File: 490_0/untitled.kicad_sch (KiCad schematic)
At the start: 30 parts, among them J2 BM04B-PASS-1-TFT, J3 BM04B-PASS-1-TFT, U4 USB2512B-I/M2, Y1 24 MHz

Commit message: Changed 8conn and BOM update
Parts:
- C17, C18: footprint (none) -> Capacitor_SMD:C_0603_1608Metric
- C53, C54, C56, C57, C58, C59, C60, C61, C62: footprint (none) -> Capacitor_SMD:C_0805_2012Metric
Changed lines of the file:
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@@
 			)
 		)
-		(property "Footprint" ""
+		(property "Footprint" "Capacitor_SMD:C_0805_2012Metric"
 			(at 177.8 88.9 0)
 			(effects
@@
 			)
 		)
-		(property "Footprint" ""
+		(property "Footprint" "Capacitor_SMD:C_0805_2012Metric"
 			(at 88.9 88.9 0)
 			(effects
@@
 			)
 		)
-		(property "Footprint" ""
+		(property "Footprint" "Capacitor_SMD:C_0805_2012Metric"
 			(at 53.34 88.9 0)
 			(effects
@@
 			)
 		)
-		(property "Footprint" ""
+		(property "Footprint" "Capacitor_SMD:C_0805_2012Metric"
 			(at 81.28 142.24 0)
 			(effects
@@
 			)
 		)
-		(property "Footprint" ""
+		(property "Footprint" "Capacitor_SMD:C_0805_2012Metric"
 			(at 66.04 78.74 0)
 			(effects
@@
 			)
 		)
-		(property "Footprint" ""
+		(property "Footprint" "Capacitor_SMD:C_0805_2012Metric"
 			(at 81.28 137.16 0)
 			(effects
@@
 			)
 		)
-		(property "Footprint" ""
+		(property "Footprint" "Capacitor_SMD:C_0805_2012Metric"
 			(at 73.66 88.9 0)
 			(effects
@@
 			)
 		)
-		(property "Footprint" ""
+		(property "Footprint" "Capacitor_SMD:C_0805_2012Metric"
 			(at 185.42 78.74 0)
 			(effects
@@
 			)
 		)
-		(property "Footprint" ""
+		(property "Footprint" "Capacitor_SMD:C_0603_1608Metric"
 			(at 33.02 152.4 0)
 			(effects
@@
 			)
 		)
-		(property "Footprint" ""
+		(property "Footprint" "Capacitor_SMD:C_0805_2012Metric"
 			(at 81.28 78.74 0)
 			(effects
@@
 			)
 		)
-		(property "Footprint" ""
+		(property "Footprint" "Capacitor_SMD:C_0603_1608Metric"
 			(at 17.78 152.4 0)
 			(effects

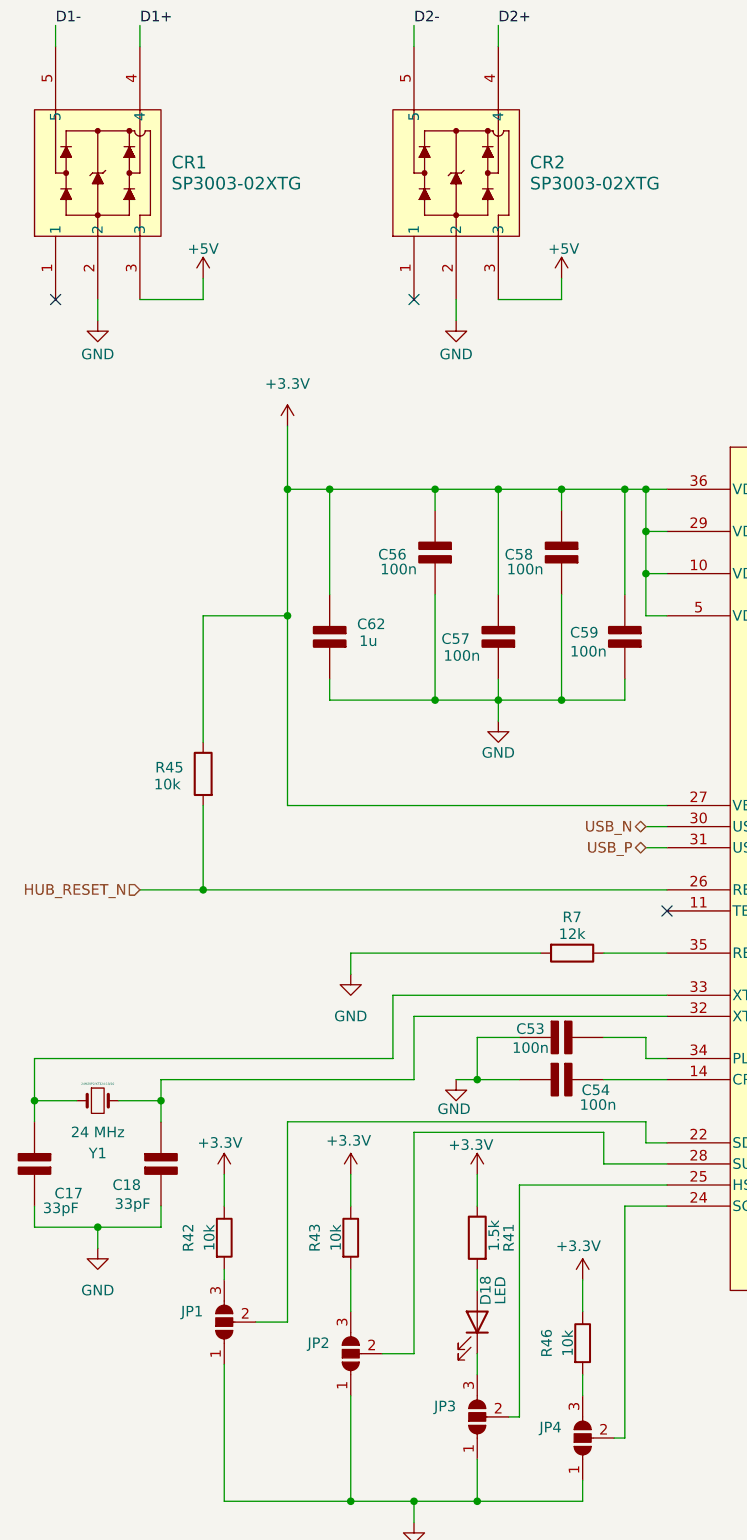
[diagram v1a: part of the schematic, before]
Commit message: LED names + 5V routing through ESD + renamed ESD chips to "U"
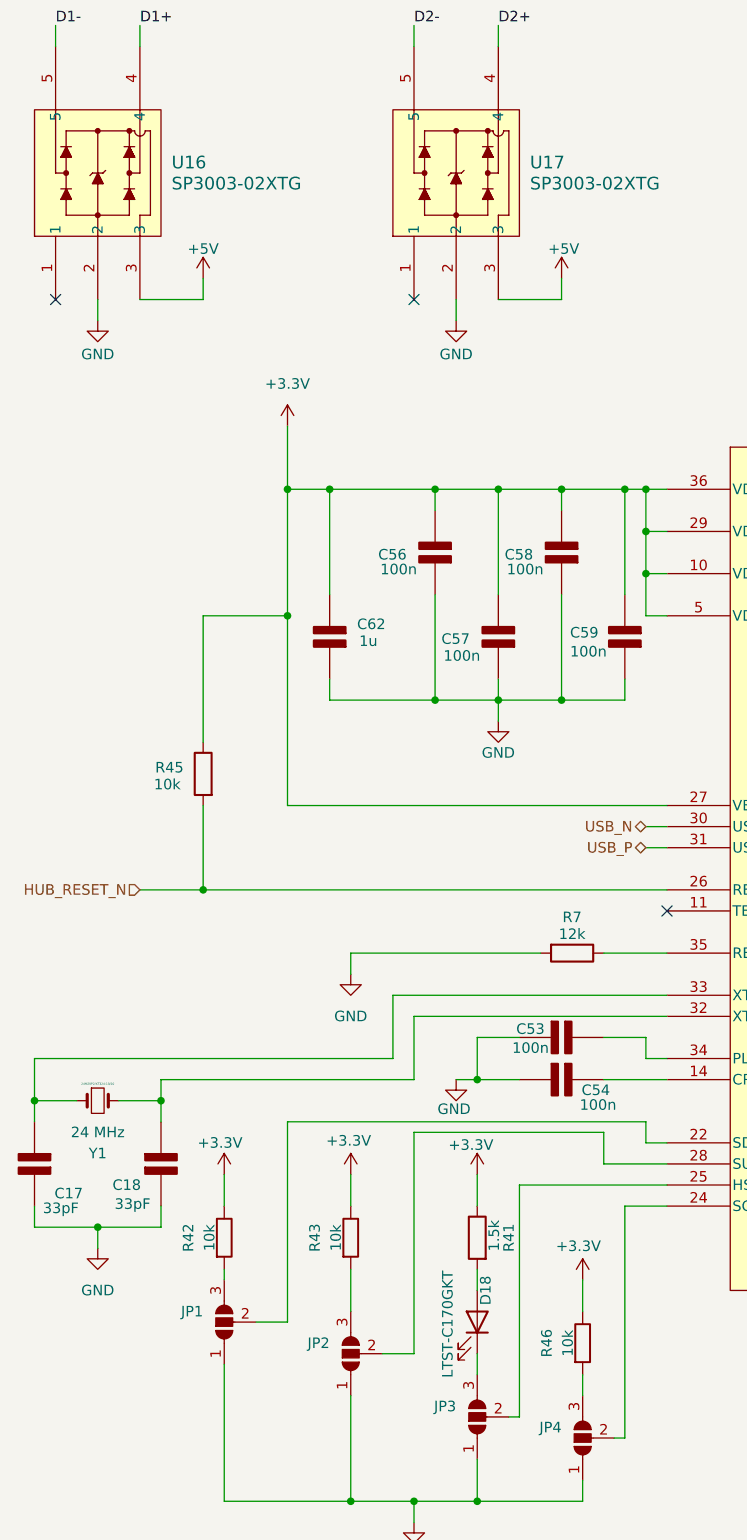
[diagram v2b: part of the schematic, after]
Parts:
- D18: value LED -> LTST-C170GKT
- renumbered CR1 to U16, CR2 to U17
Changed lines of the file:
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@@
 		(dnp no)
 		(fields_autoplaced yes)
-		(property "Reference" "CR1"
+		(property "Reference" "U16"
 			(at 34.29 31.7499 90)
 			(effects
@@
 			(project "490_0"
 				(path "/365a82ed-827d-43e1-aa2f-b98221c4179c/a8971e06-9d2b-4df6-83ab-783791bb1c3f/068f11fb-720d-48b0-8797-6d8a5a01cc51"
-					(reference "CR1")
+					(reference "U16")
 					(unit 1)
 				)
@@
 		(dnp no)
 		(fields_autoplaced yes)
-		(property "Reference" "CR2"
+		(property "Reference" "U17"
 			(at 77.47 31.7499 90)
 			(effects
@@
 			(project "490_0"
 				(path "/365a82ed-827d-43e1-aa2f-b98221c4179c/a8971e06-9d2b-4df6-83ab-783791bb1c3f/068f11fb-720d-48b0-8797-6d8a5a01cc51"
-					(reference "CR2")
+					(reference "U17")
 					(unit 1)
 				)
@@
 			)
 		)
-		(property "Value" "LED"
-			(at 73.914 167.64 0)
+		(property "Value" "LTST-C170GKT"
+			(at 67.564 171.704 0)
 			(effects
 				(font

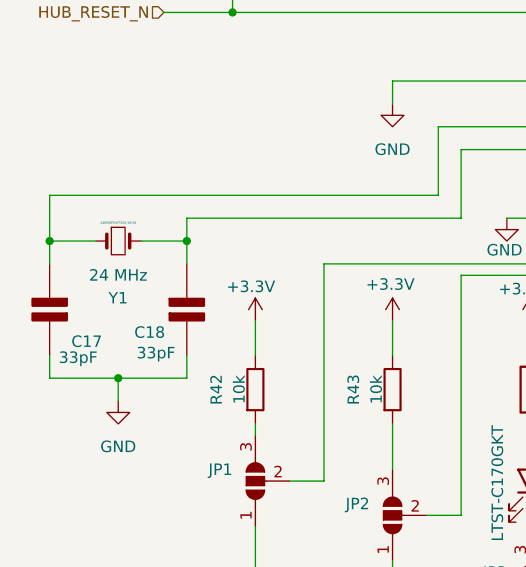
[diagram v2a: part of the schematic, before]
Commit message: Renamed crystal + BOM update
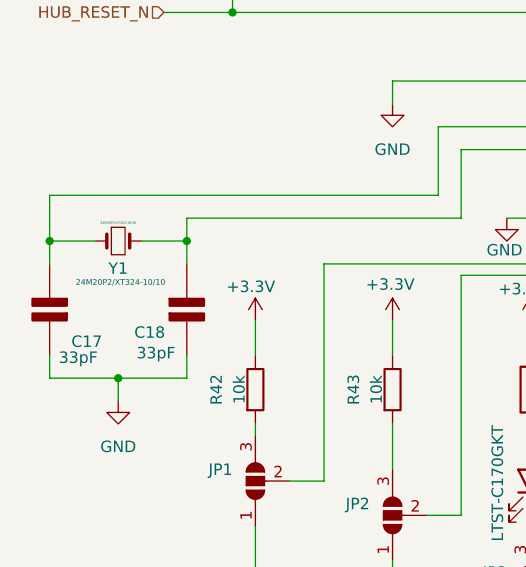
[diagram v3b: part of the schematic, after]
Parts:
- Y1: value 24 MHz -> 24M20P2/XT324-10/10
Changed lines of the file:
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@@
 		(dnp no)
 		(property "Reference" "Y1"
-			(at 25.4 151.13 0)
+			(at 25.4 147.828 0)
 			(effects
 				(font
@@
 			)
 		)
-		(property "Value" "24 MHz"
-			(at 25.4 148.59 0)
+		(property "Value" "24M20P2/XT324-10/10"
+			(at 25.654 149.352 0)
 			(effects
 				(font
-					(size 1.27 1.27)
+					(size 0.635 0.635)
 				)
 			)

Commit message: Post-Dmitry Changes
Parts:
- added R11: 330, Resistor_THT:R_Axial_DIN0207_L6.3mm_D2.5mm_P10.16mm_Horizontal, symbol PCM_SL_Resistors:Resistor
- J2, J3: footprint *CapStone*:CONN_BM04B-PASS-1-TFTLFSN_JST -> Connector_PinHeader_1.27mm:PinHeader_1x04_P1.27mm_Vertical
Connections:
- net GND: now also R11.1
- net at JP3.2 (C), U4.25 (HS_IND/CFG_SEL1): now also R11.2
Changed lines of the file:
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@@
 	)
 	(junction
+		(at 76.2 193.04)
+		(diameter 0)
+		(color 0 0 0 0)
+	)
+	(junction
 		(at 177.8 81.28)
 		(diameter 0)
@@
 	)
 	(junction
+		(at 76.2 182.88)
+		(diameter 0)
+		(color 0 0 0 0)
+	)
+	(junction
 		(at 48.26 71.12)
 		(diameter 0)
@@
 	(wire
 		(pts
+			(xy 76.2 193.04) (xy 71.12 193.04)
+		)
+		(stroke
+			(width 0)
+			(type default)
+		)
+	)
+	(wire
+		(pts
 			(xy 40.64 176.53) (xy 40.64 193.04)
 		)
@@
 	(wire
 		(pts
+			(xy 76.2 190.5) (xy 76.2 193.04)
+		)
+		(stroke
+			(width 0)
+			(type default)
+		)
+	)
+	(wire
+		(pts
 			(xy 76.2 182.88) (xy 76.2 154.94)
 		)
@@
 	(wire
 		(pts
-			(xy 83.82 193.04) (xy 71.12 193.04)
+			(xy 83.82 193.04) (xy 76.2 193.04)
 		)
 		(stroke
@@
 			)
 		)
-		(property "Footprint" "*CapStone*:CONN_BM04B-PASS-1-TFTLFSN_JST"
+		(property "Footprint" "Connector_PinHeader_1.27mm:PinHeader_1x04_P1.27mm_Vertical"
 			(at 231.14 154.94 0)
 			(effects
@@
 			)
 		)
-		(property "Footprint" "*CapStone*:CONN_BM04B-PASS-1-TFTLFSN_JST"
+		(property "Footprint" "Connector_PinHeader_1.27mm:PinHeader_1x04_P1.27mm_Vertical"
 			(at 231.14 124.46 0)
 			(effects
@@
 					(unit 1)
 				)
+			)
+		)
+	)
+	(symbol
+		(lib_id "PCM_SL_Resistors:Resistor")
+		(at 76.2 186.69 90)
+		(unit 1)
+		(exclude_from_sim no)
+		(in_bom yes)
+		(on_board yes)
+		(dnp no)
+		(property "Reference" "R11"
+			(at 71.882 186.69 0)
+			(effects
+				(font
+					(size 1.27 1.27)
+				)
+			)
+		)
+		(property "Value" "330"
+			(at 74.422 186.69 0)
+			(effects
+				(font
+					(size 1.27 1.27)
+				)
+			)
+		)
+		(property "Footprint" "Resistor_THT:R_Axial_DIN0207_L6.3mm_D2.5mm_P10.16mm_Horizontal"
+			(at 80.518 185.801 0)
+			(effects
+				(font
+					(size 1.27 1.27)
+				)
+				(hide yes)
+			)
+		)
+		(property "Datasheet" "kicad-embed://PYU-RC_GROUP_51_ROHS_L (YAGEO resistors).pdf"
+			(at 76.2 186.182 0)
+			(effects
+				(font
+					(size 1.27 1.27)
+				)
+				(hide yes)
+			)
+		)
+		(property "Description" "RES 10K OHM 1% 1/4W 1206"
+			(at 76.2 186.69 0)
+			(effects
+				(font
+					(size 1.27 1.27)
+				)
+				(hide yes)
+			)
+		)
+		(property "Digikey Link" "https://www.digikey.ca/en/products/detail/yageo/RC1206FR-0710KL/728483"
+			(at 76.2 186.69 0)
+			(effects
+				(font
+					(size 1.27 1.27)
+				)
+				(hide yes)
+			)
+		)
+		(property "Manufacturer" "YAGEO"
+			(at 76.2 186.69 0)
+			(effects
+				(font
+					(size 1.27 1.27)
+				)
+				(hide yes)
+			)
+		)
+		(property "Manufacturer Part" "RC1206FR-0710KL"
+			(at 76.2 186.69 0)
+			(effects
+				(font
+					(size 1.27 1.27)
+				)
+				(hide yes)
+			)
+		)
+		(property "Package" "1206"
+			(at 76.2 186.69 0)
+			(effects
+				(font
+					(size 1.27 1.27)
+				)
+				(hide yes)
+			)
+		)
+		(property "Price" "0.1"
+			(at 76.2 186.69 0)
+			(effects
+				(font
+					(size 1.27 1.27)
+				)
+				(hide yes)
+			)
+		)
+		(property "Supplier" "DigiKey"
+			(at 76.2 186.69 0)
+			(effects
+				(font
+					(size 1.27 1.27)
+				)
+				(hide yes)
+			)
+		)
+		(property "Supplier P/N" "311-10.0KFRCT-ND"
+			(at 76.2 186.69 0)
+			(effects
+				(font
+					(size 1.27 1.27)
+				)
+				(hide yes)
+			)
+		)
+		(property "Type" "SMD"
+			(at 76.2 186.69 0)
+			(effects
+				(font
+					(size 1.27 1.27)
+				)
+				(hide yes)
+			)
+		)
+		(property "Unit" "pcs"
+			(at 76.2 186.69 0)
+			(effects
+				(font
+					(size 1.27 1.27)
+				)
+				(hide yes)
+			)
+		)
+		(pin "1"
+		)
+		(pin "2"
+		)
+		(instances
+			(project "490_0"
+				(path "/365a82ed-827d-43e1-aa2f-b98221c4179c/a8971e06-9d2b-4df6-83ab-783791bb1c3f/068f11fb-720d-48b0-8797-6d8a5a01cc51"
+					(reference "R11")
+					(unit 1)
+				)

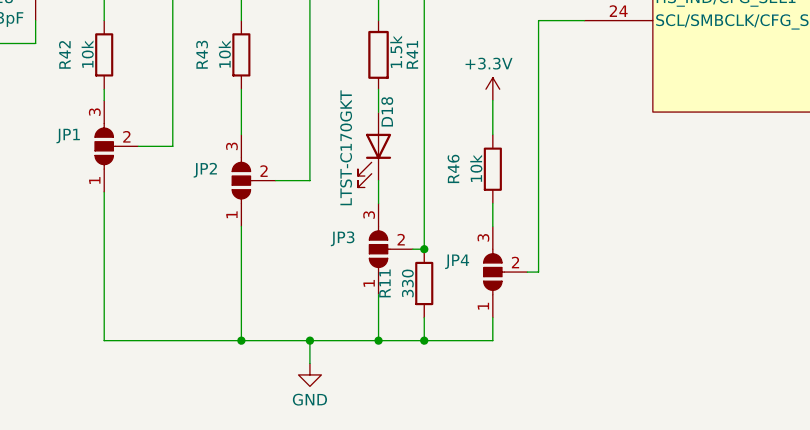
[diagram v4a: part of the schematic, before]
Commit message: Added seperate ground for PWM motors
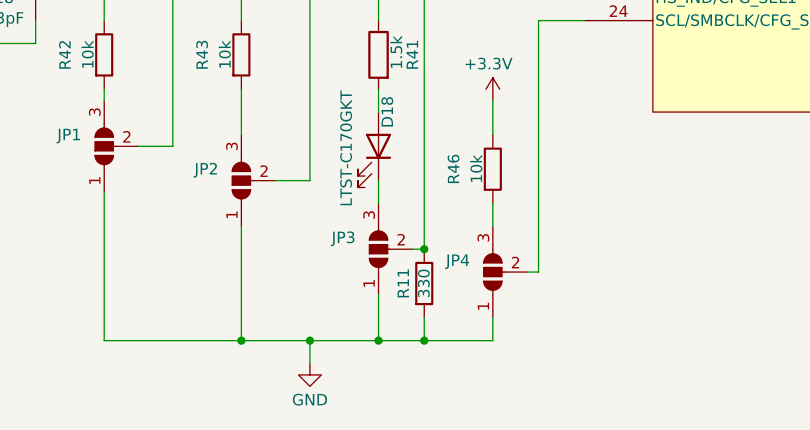
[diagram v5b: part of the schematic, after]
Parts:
- R11: Unit pcs -> (none)
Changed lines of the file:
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@@
 		(dnp no)
 		(property "Reference" "R11"
-			(at 71.882 186.69 0)
+			(at 73.914 186.69 0)
 			(effects
 				(font
@@
 		)
 		(property "Value" "330"
-			(at 74.422 186.69 0)
+			(at 76.2 186.69 0)
 			(effects
 				(font
@@
 			)
 		)
-		(property "Unit" "pcs"
+		(property "Unit" ""
 			(at 76.2 186.69 0)
 			(effects

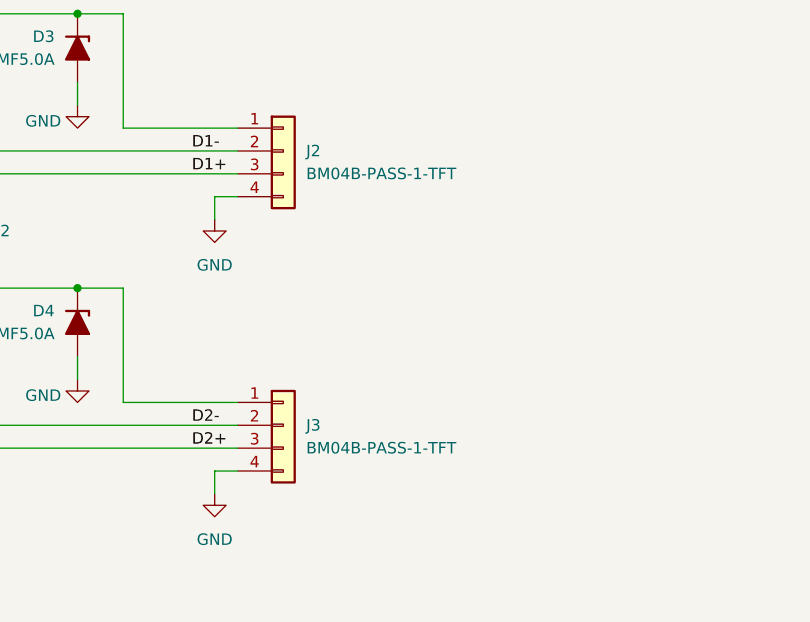
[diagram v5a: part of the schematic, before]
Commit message: Changed footprints for pad connectors (for soldered components)
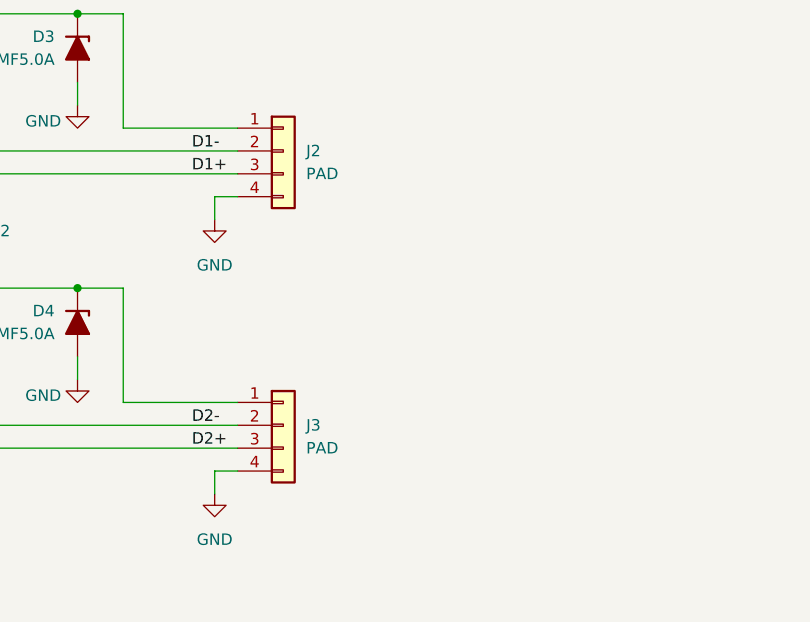
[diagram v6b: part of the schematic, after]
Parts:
- J2, J3: value BM04B-PASS-1-TFT -> PAD
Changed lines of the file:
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@@
 			)
 		)
-		(property "Value" "BM04B-PASS-1-TFT"
+		(property "Value" "PAD"
 			(at 233.68 147.3199 0)
 			(effects
@@
 			)
 		)
-		(property "Value" "BM04B-PASS-1-TFT"
+		(property "Value" "PAD"
 			(at 233.68 116.8399 0)
 			(effects
